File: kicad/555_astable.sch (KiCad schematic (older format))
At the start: 10 parts, among them U2 555

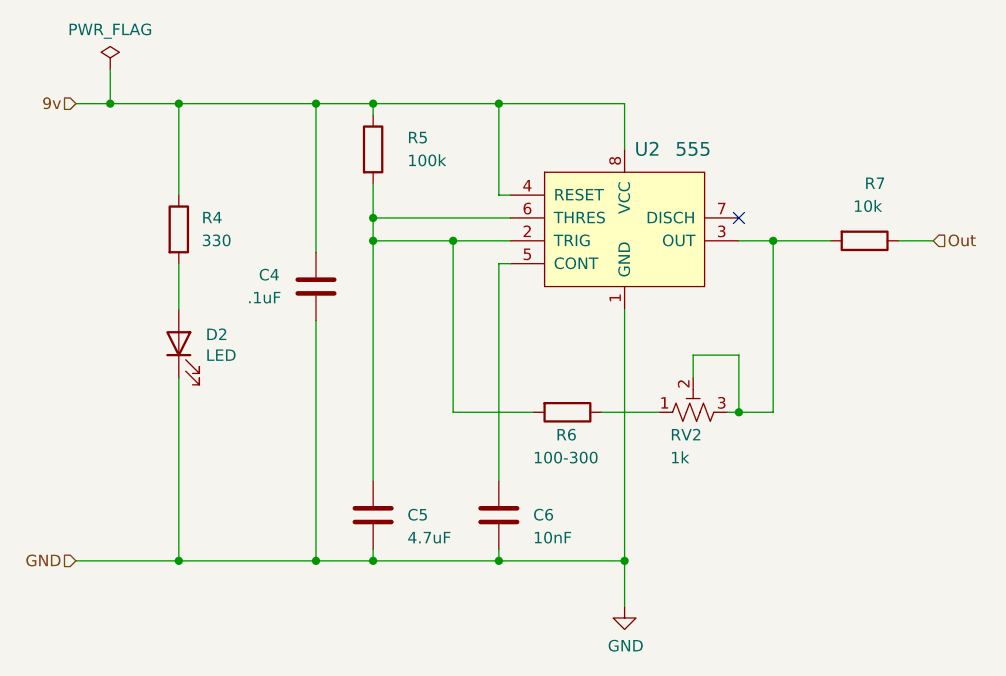
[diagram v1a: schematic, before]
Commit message: PCB revisions:
* Fix APC ground error
* Add voltage regulator to POLY_555
* Ditch hitch
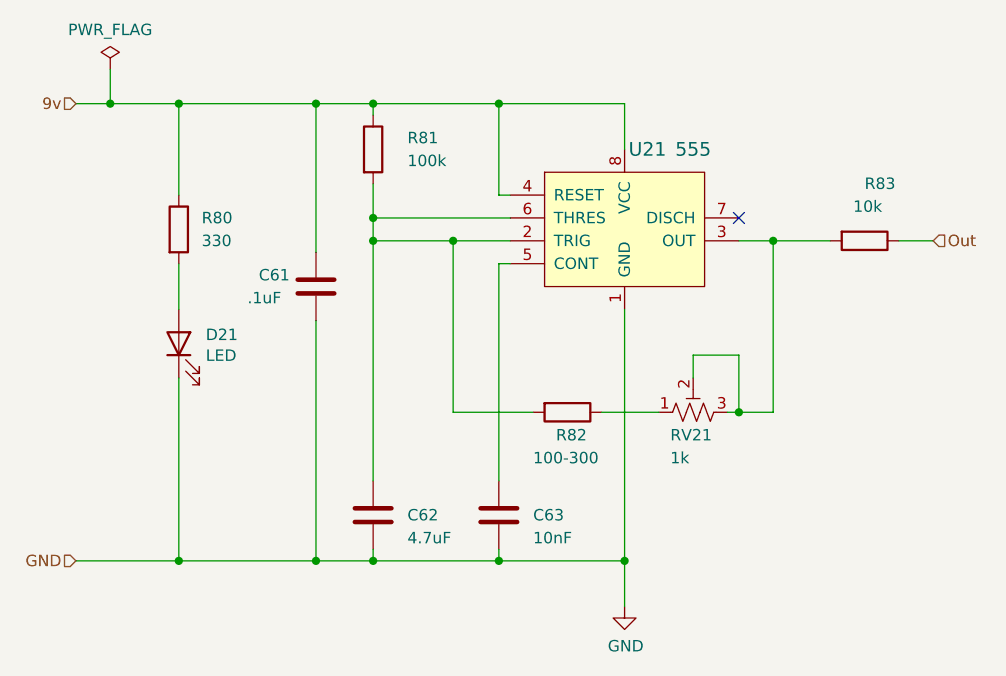
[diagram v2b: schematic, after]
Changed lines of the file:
@@
 AR Path="/5F842C45/60F6A68E" Ref="R77"  Part="1"
 AR Path="/5F842C61/60F6A68E" Ref="R81"  Part="1"
-F 0 "R5" H 4750 3500 50  0000 L CNN
+F 0 "R81" H 4750 3500 50  0000 L CNN
 F 1 "100k" H 4750 3400 50  0000 L CNN
 F 2 "Resistor_THT:R_Axial_DIN0207_L6.3mm_D2.5mm_P2.54mm_Vertical" V 4530 3450 50  0001 C CNN
@@
 AR Path="/5F842C45/60F6EAC0" Ref="C58"  Part="1"
 AR Path="/5F842C61/60F6EAC0" Ref="C61"  Part="1"
-F 0 "C4" H 4100 4100 50  0000 L CNN
+F 0 "C61" H 4100 4100 50  0000 L CNN
 F 1 ".1uF" H 4050 4000 50  0000 L CNN
 F 2 "Capacitor_THT:C_Disc_D5.0mm_W2.5mm_P5.00mm" H 4388 3900 50  0001 C CNN
@@
 	1    0    0    -1
 $EndComp
-Text HLabel 3300 3250 0    50   Input ~ 0
-9v
 Wire Wire Line
 	4600 3250 4350 3250
@@
 AR Path="/5F842C45/60F6A6DA" Ref="U20"  Part="1"
 AR Path="/5F842C61/60F6A6DA" Ref="U21"  Part="1"
-F 0 "U2" H 5800 4050 60  0000 C CNN
+F 0 "U21" H 5800 4050 60  0000 C CNN
 F 1 "555" H 6000 4050 60  0000 C CNN
 F 2 "Package_DIP:DIP-8_W7.62mm" H 5900 3950 60  0001 L CNN
@@
 AR Path="/5F842C45/60F6A6C5" Ref="RV20"  Part="1"
 AR Path="/5F842C61/60F6A6C5" Ref="RV21"  Part="1"
-F 0 "RV2" V 5900 4700 50  0000 R CNN
+F 0 "RV21" V 5900 4700 50  0000 R CNN
 F 1 "1k" V 5800 4700 50  0000 R CNN
 F 2 "Potentiometer_THT:Potentiometer_Piher_PT-6-V_Vertical" H 6000 4600 50  0001 C CNN
@@
 AR Path="/5F842C45/5EFAE830" Ref="R79"  Part="1"
 AR Path="/5F842C61/5EFAE830" Ref="R83"  Part="1"
-F 0 "R7" V 6500 3850 50  0000 L CNN
+F 0 "R83" V 6500 3850 50  0000 L CNN
 F 1 "10k" V 6600 3800 50  0000 L CNN
 F 2 "Resistor_THT:R_Axial_DIN0207_L6.3mm_D2.5mm_P2.54mm_Vertical" V 6680 3850 50  0001 C CNN
@@
 AR Path="/5F842C45/5F127BEF" Ref="D20"  Part="1"
 AR Path="/5F842C61/5F127BEF" Ref="D21"  Part="1"
-F 0 "D2" V 3789 4182 50  0000 R CNN
+F 0 "D21" V 3789 4182 50  0000 R CNN
 F 1 "LED" V 3698 4182 50  0000 R CNN
 F 2 "LED_THT:LED_D5.0mm" H 3750 4300 50  0001 C CNN
@@
 AR Path="/5F842C45/5F127BF5" Ref="R76"  Part="1"
 AR Path="/5F842C61/5F127BF5" Ref="R80"  Part="1"
-F 0 "R4" H 3850 3850 50  0000 L CNN
+F 0 "R80" H 3850 3850 50  0000 L CNN
 F 1 "330" H 3850 3750 50  0000 L CNN
 F 2 "Resistor_THT:R_Axial_DIN0207_L6.3mm_D2.5mm_P2.54mm_Vertical" V 3680 3800 50  0001 C CNN
@@
 AR Path="/5F842C45/60F6A6A0" Ref="C60"  Part="1"
 AR Path="/5F842C61/60F6A6A0" Ref="C63"  Part="1"
-F 0 "C6" H 5300 5050 50  0000 L CNN
+F 0 "C63" H 5300 5050 50  0000 L CNN
 F 1 "10nF" H 5300 4950 50  0000 L CNN
 F 2 "Capacitor_THT:C_Disc_D5.0mm_W2.5mm_P5.00mm" H 5188 4900 50  0001 C CNN
@@
 AR Path="/5F842C45/60F6A69A" Ref="C59"  Part="1"
 AR Path="/5F842C61/60F6A69A" Ref="C62"  Part="1"
-F 0 "C5" H 4750 5050 50  0000 L CNN
+F 0 "C62" H 4750 5050 50  0000 L CNN
 F 1 "4.7uF" H 4750 4950 50  0000 L CNN
 F 2 "Capacitor_THT:CP_Radial_D4.0mm_P2.00mm" H 4638 4900 50  0001 C CNN
@@
 AR Path="/5F842C45/5F3F39A8" Ref="R78"  Part="1"
 AR Path="/5F842C61/5F3F39A8" Ref="R82"  Part="1"
-F 0 "R6" V 5550 4550 50  0000 L CNN
+F 0 "R82" V 5550 4550 50  0000 L CNN
 F 1 "100-300" V 5650 4450 50  0000 L CNN
 F 2 "Resistor_THT:R_Axial_DIN0207_L6.3mm_D2.5mm_P2.54mm_Vertical" V 5380 4600 50  0001 C CNN
@@
 	0    1    1    0
 $EndComp
+Text HLabel 3300 3250 0    50   Input ~ 0
+9v
 $EndSCHEMATC

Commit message: Reorder components left to right
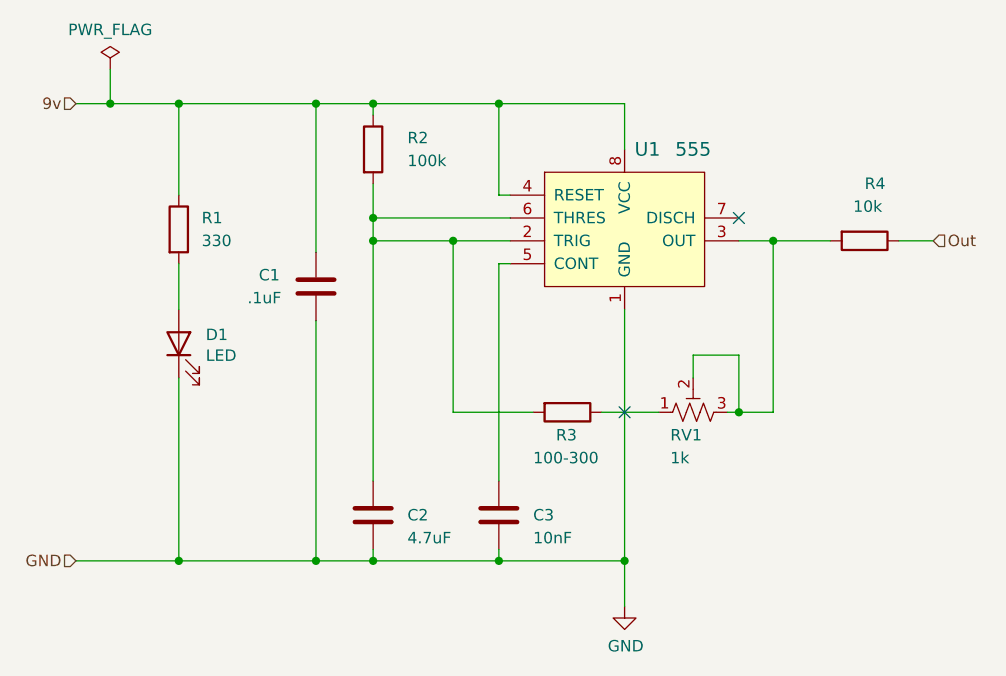
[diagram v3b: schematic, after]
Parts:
- renumbered C4 to C1, C5 to C2, C6 to C3, D2 to D1, R4 to R1, R5 to R2, R6 to R3, R7 to R4, RV2 to RV1, U2 to U1
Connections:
- no-connect marks 1 -> 2

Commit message: APC fixes
* Reverse volume pot direction
* Reroute
* Swap timing cap footprint
* Add stress relief hole for battery wires
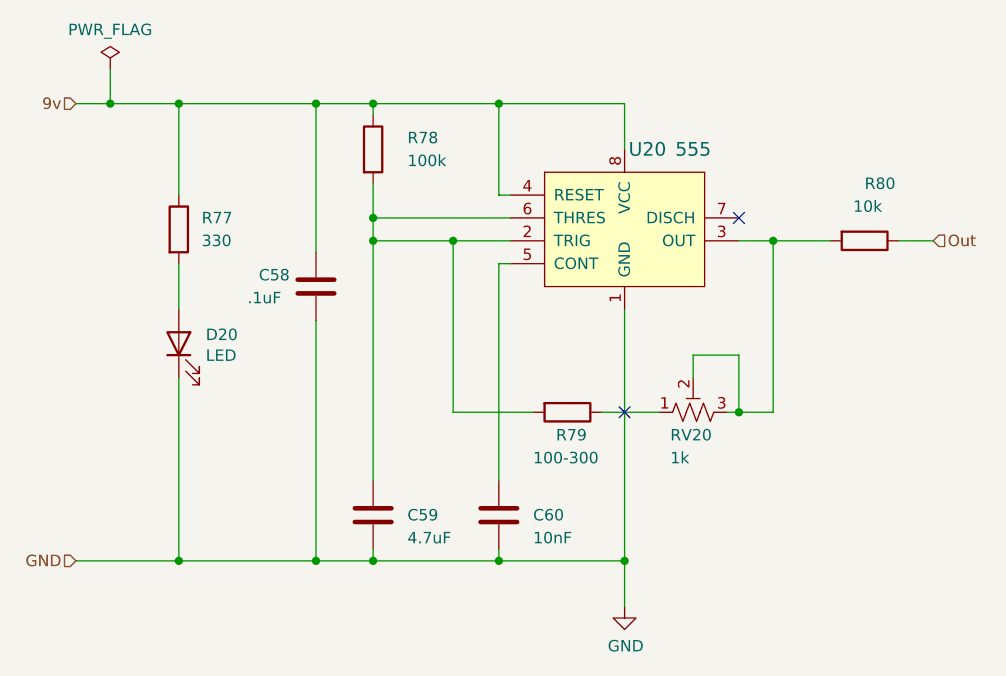
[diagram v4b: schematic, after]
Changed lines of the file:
@@
 $Descr A4 11693 8268
 encoding utf-8
-Sheet 2 22
+Sheet 21 22
 Title ""
 Date ""
@@
 AR Path="/5F842C45/60F6A68E" Ref="R74"  Part="1"
 AR Path="/5F842C61/60F6A68E" Ref="R78"  Part="1"
-F 0 "R2" H 4750 3500 50  0000 L CNN
+F 0 "R78" H 4750 3500 50  0000 L CNN
 F 1 "100k" H 4750 3400 50  0000 L CNN
 F 2 "Resistor_THT:R_Axial_DIN0207_L6.3mm_D2.5mm_P2.54mm_Vertical" V 4530 3450 50  0001 C CNN
@@
 AR Path="/5F842C45/60F6EAC0" Ref="C55"  Part="1"
 AR Path="/5F842C61/60F6EAC0" Ref="C58"  Part="1"
-F 0 "C1" H 4100 4100 50  0000 L CNN
+F 0 "C58" H 4100 4100 50  0000 L CNN
 F 1 ".1uF" H 4050 4000 50  0000 L CNN
 F 2 "Capacitor_THT:C_Disc_D5.0mm_W2.5mm_P5.00mm" H 4388 3900 50  0001 C CNN
@@
 AR Path="/5F842C45/60F6A6DA" Ref="U19"  Part="1"
 AR Path="/5F842C61/60F6A6DA" Ref="U20"  Part="1"
-F 0 "U1" H 5800 4050 60  0000 C CNN
+F 0 "U20" H 5800 4050 60  0000 C CNN
 F 1 "555" H 6000 4050 60  0000 C CNN
 F 2 "Package_DIP:DIP-8_W7.62mm" H 5900 3950 60  0001 L CNN
@@
 AR Path="/5F842C45/60F6A6C5" Ref="RV19"  Part="1"
 AR Path="/5F842C61/60F6A6C5" Ref="RV20"  Part="1"
-F 0 "RV1" V 5900 4700 50  0000 R CNN
+F 0 "RV20" V 5900 4700 50  0000 R CNN
 F 1 "1k" V 5800 4700 50  0000 R CNN
 F 2 "Potentiometer_THT:Potentiometer_Piher_PT-6-V_Vertical" H 6000 4600 50  0001 C CNN
@@
 AR Path="/5F842C45/5EFAE830" Ref="R76"  Part="1"
 AR Path="/5F842C61/5EFAE830" Ref="R80"  Part="1"
-F 0 "R4" V 6500 3850 50  0000 L CNN
+F 0 "R80" V 6500 3850 50  0000 L CNN
 F 1 "10k" V 6600 3800 50  0000 L CNN
 F 2 "Resistor_THT:R_Axial_DIN0207_L6.3mm_D2.5mm_P2.54mm_Vertical" V 6680 3850 50  0001 C CNN
@@
 AR Path="/5F842C45/5F127BEF" Ref="D19"  Part="1"
 AR Path="/5F842C61/5F127BEF" Ref="D20"  Part="1"
-F 0 "D1" V 3789 4182 50  0000 R CNN
+F 0 "D20" V 3789 4182 50  0000 R CNN
 F 1 "LED" V 3698 4182 50  0000 R CNN
 F 2 "LED_THT:LED_D5.0mm" H 3750 4300 50  0001 C CNN
@@
 AR Path="/5F842C45/5F127BF5" Ref="R73"  Part="1"
 AR Path="/5F842C61/5F127BF5" Ref="R77"  Part="1"
-F 0 "R1" H 3850 3850 50  0000 L CNN
+F 0 "R77" H 3850 3850 50  0000 L CNN
 F 1 "330" H 3850 3750 50  0000 L CNN
 F 2 "Resistor_THT:R_Axial_DIN0207_L6.3mm_D2.5mm_P2.54mm_Vertical" V 3680 3800 50  0001 C CNN
@@
 AR Path="/5F842C45/60F6A6A0" Ref="C57"  Part="1"
 AR Path="/5F842C61/60F6A6A0" Ref="C60"  Part="1"
-F 0 "C3" H 5300 5050 50  0000 L CNN
+F 0 "C60" H 5300 5050 50  0000 L CNN
 F 1 "10nF" H 5300 4950 50  0000 L CNN
 F 2 "Capacitor_THT:C_Disc_D5.0mm_W2.5mm_P5.00mm" H 5188 4900 50  0001 C CNN
@@
 AR Path="/5F842C45/60F6A69A" Ref="C56"  Part="1"
 AR Path="/5F842C61/60F6A69A" Ref="C59"  Part="1"
-F 0 "C2" H 4750 5050 50  0000 L CNN
+F 0 "C59" H 4750 5050 50  0000 L CNN
 F 1 "4.7uF" H 4750 4950 50  0000 L CNN
 F 2 "Capacitor_THT:CP_Radial_D4.0mm_P2.00mm" H 4638 4900 50  0001 C CNN
@@
 AR Path="/5F842C45/5F3F39A8" Ref="R75"  Part="1"
 AR Path="/5F842C61/5F3F39A8" Ref="R79"  Part="1"
-F 0 "R3" V 5550 4550 50  0000 L CNN
+F 0 "R79" V 5550 4550 50  0000 L CNN
 F 1 "100-300" V 5650 4450 50  0000 L CNN
 F 2 "Resistor_THT:R_Axial_DIN0207_L6.3mm_D2.5mm_P2.54mm_Vertical" V 5380 4600 50  0001 C CNN

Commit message: Swap 4.7uF cap footprints and re-route
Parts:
- C2: footprint Capacitor_THT:CP_Radial_D4.0mm_P2.00mm -> Capacitor_THT:CP_Radial_D5.0mm_P2.00mm
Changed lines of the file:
@@
 F 0 "C59" H 4750 5050 50  0000 L CNN
 F 1 "4.7uF" H 4750 4950 50  0000 L CNN
-F 2 "Capacitor_THT:CP_Radial_D4.0mm_P2.00mm" H 4638 4900 50  0001 C CNN
+F 2 "Capacitor_THT:CP_Radial_D5.0mm_P2.00mm" H 4638 4900 50  0001 C CNN
 F 3 "~" H 4600 5050 50  0001 C CNN
 F 4 "Timing" H 4600 5050 50  0001 C CNN "Description"

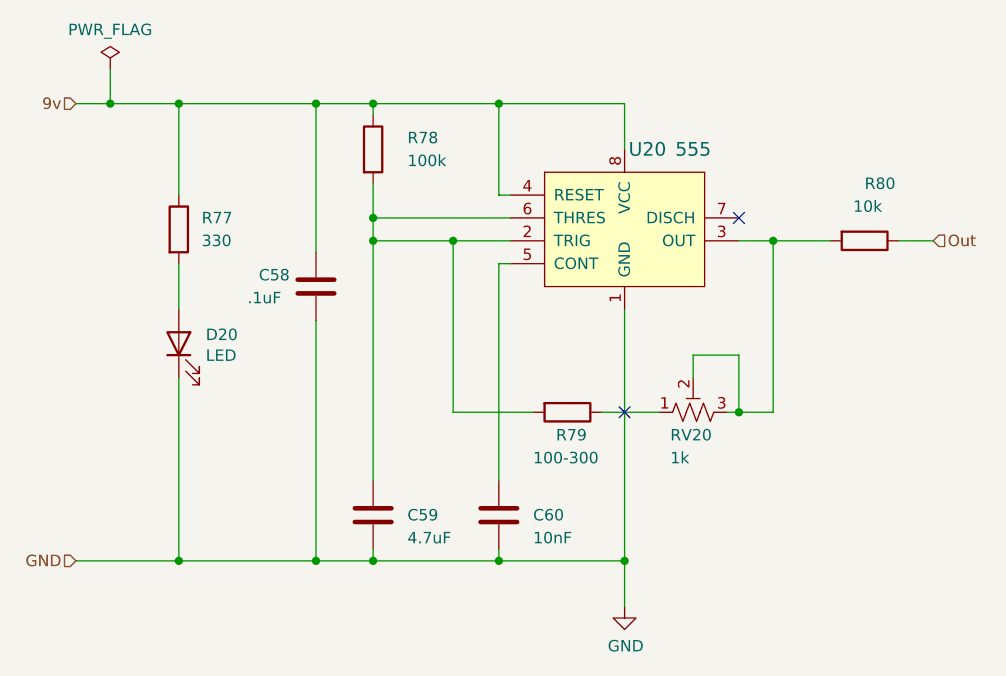
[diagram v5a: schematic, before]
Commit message: Upgrade APC pots and re-route
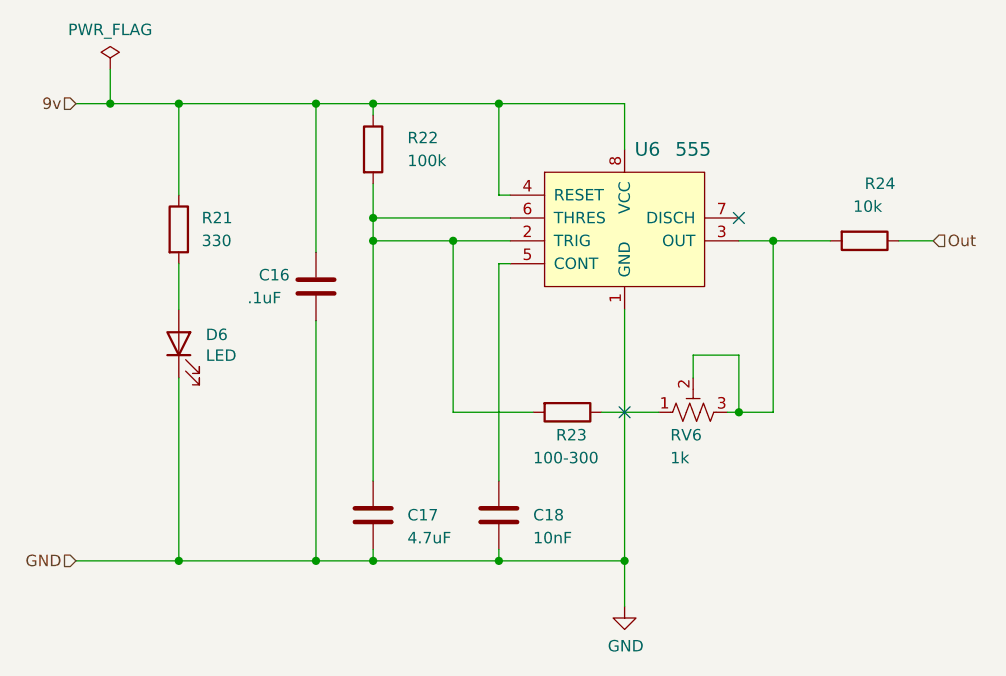
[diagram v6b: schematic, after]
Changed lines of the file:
@@
 $Descr A4 11693 8268
 encoding utf-8
-Sheet 21 22
+Sheet 7 22
 Title ""
 Date ""
@@
 AR Path="/5F842C45/60F6A68E" Ref="R74"  Part="1"
 AR Path="/5F842C61/60F6A68E" Ref="R78"  Part="1"
-F 0 "R78" H 4750 3500 50  0000 L CNN
+F 0 "R22" H 4750 3500 50  0000 L CNN
 F 1 "100k" H 4750 3400 50  0000 L CNN
 F 2 "Resistor_THT:R_Axial_DIN0207_L6.3mm_D2.5mm_P2.54mm_Vertical" V 4530 3450 50  0001 C CNN
@@
 AR Path="/5F842C45/60F6EAC0" Ref="C55"  Part="1"
 AR Path="/5F842C61/60F6EAC0" Ref="C58"  Part="1"
-F 0 "C58" H 4100 4100 50  0000 L CNN
+F 0 "C16" H 4100 4100 50  0000 L CNN
 F 1 ".1uF" H 4050 4000 50  0000 L CNN
 F 2 "Capacitor_THT:C_Disc_D5.0mm_W2.5mm_P5.00mm" H 4388 3900 50  0001 C CNN
@@
 AR Path="/5F842C45/60F6A6DA" Ref="U19"  Part="1"
 AR Path="/5F842C61/60F6A6DA" Ref="U20"  Part="1"
-F 0 "U20" H 5800 4050 60  0000 C CNN
+F 0 "U6" H 5800 4050 60  0000 C CNN
 F 1 "555" H 6000 4050 60  0000 C CNN
 F 2 "Package_DIP:DIP-8_W7.62mm" H 5900 3950 60  0001 L CNN
@@
 AR Path="/5F842C45/60F6A6C5" Ref="RV19"  Part="1"
 AR Path="/5F842C61/60F6A6C5" Ref="RV20"  Part="1"
-F 0 "RV20" V 5900 4700 50  0000 R CNN
+F 0 "RV6" V 5900 4700 50  0000 R CNN
 F 1 "1k" V 5800 4700 50  0000 R CNN
 F 2 "Potentiometer_THT:Potentiometer_Piher_PT-6-V_Vertical" H 6000 4600 50  0001 C CNN
@@
 AR Path="/5F842C45/5EFAE830" Ref="R76"  Part="1"
 AR Path="/5F842C61/5EFAE830" Ref="R80"  Part="1"
-F 0 "R80" V 6500 3850 50  0000 L CNN
+F 0 "R24" V 6500 3850 50  0000 L CNN
 F 1 "10k" V 6600 3800 50  0000 L CNN
 F 2 "Resistor_THT:R_Axial_DIN0207_L6.3mm_D2.5mm_P2.54mm_Vertical" V 6680 3850 50  0001 C CNN
@@
 AR Path="/5F842C45/5F127BEF" Ref="D19"  Part="1"
 AR Path="/5F842C61/5F127BEF" Ref="D20"  Part="1"
-F 0 "D20" V 3789 4182 50  0000 R CNN
+F 0 "D6" V 3789 4182 50  0000 R CNN
 F 1 "LED" V 3698 4182 50  0000 R CNN
 F 2 "LED_THT:LED_D5.0mm" H 3750 4300 50  0001 C CNN
@@
 AR Path="/5F842C45/5F127BF5" Ref="R73"  Part="1"
 AR Path="/5F842C61/5F127BF5" Ref="R77"  Part="1"
-F 0 "R77" H 3850 3850 50  0000 L CNN
+F 0 "R21" H 3850 3850 50  0000 L CNN
 F 1 "330" H 3850 3750 50  0000 L CNN
 F 2 "Resistor_THT:R_Axial_DIN0207_L6.3mm_D2.5mm_P2.54mm_Vertical" V 3680 3800 50  0001 C CNN
@@
 AR Path="/5F842C45/60F6A6A0" Ref="C57"  Part="1"
 AR Path="/5F842C61/60F6A6A0" Ref="C60"  Part="1"
-F 0 "C60" H 5300 5050 50  0000 L CNN
+F 0 "C18" H 5300 5050 50  0000 L CNN
 F 1 "10nF" H 5300 4950 50  0000 L CNN
 F 2 "Capacitor_THT:C_Disc_D5.0mm_W2.5mm_P5.00mm" H 5188 4900 50  0001 C CNN
@@
 AR Path="/5F842C45/60F6A69A" Ref="C56"  Part="1"
 AR Path="/5F842C61/60F6A69A" Ref="C59"  Part="1"
-F 0 "C59" H 4750 5050 50  0000 L CNN
+F 0 "C17" H 4750 5050 50  0000 L CNN
 F 1 "4.7uF" H 4750 4950 50  0000 L CNN
 F 2 "Capacitor_THT:CP_Radial_D5.0mm_P2.00mm" H 4638 4900 50  0001 C CNN
@@
 AR Path="/5F842C45/5F3F39A8" Ref="R75"  Part="1"
 AR Path="/5F842C61/5F3F39A8" Ref="R79"  Part="1"
-F 0 "R79" V 5550 4550 50  0000 L CNN
+F 0 "R23" V 5550 4550 50  0000 L CNN
 F 1 "100-300" V 5650 4450 50  0000 L CNN
 F 2 "Resistor_THT:R_Axial_DIN0207_L6.3mm_D2.5mm_P2.54mm_Vertical" V 5380 4600 50  0001 C CNN
